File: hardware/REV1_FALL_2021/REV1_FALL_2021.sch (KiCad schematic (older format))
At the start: 28 parts, among them J101 Screw_Terminal_01x02, J102 Screw_Terminal_01x02, Q101 Q_NMOS_GDS, Q102 Q_NMOS_GDS, U1 Teensy3.6_All_Pins, U2 PA16165_Breakout, U3 MPL3115A2_Breakout, U4 BNO055_Breakout, U5 RFM69HCW_Breakout

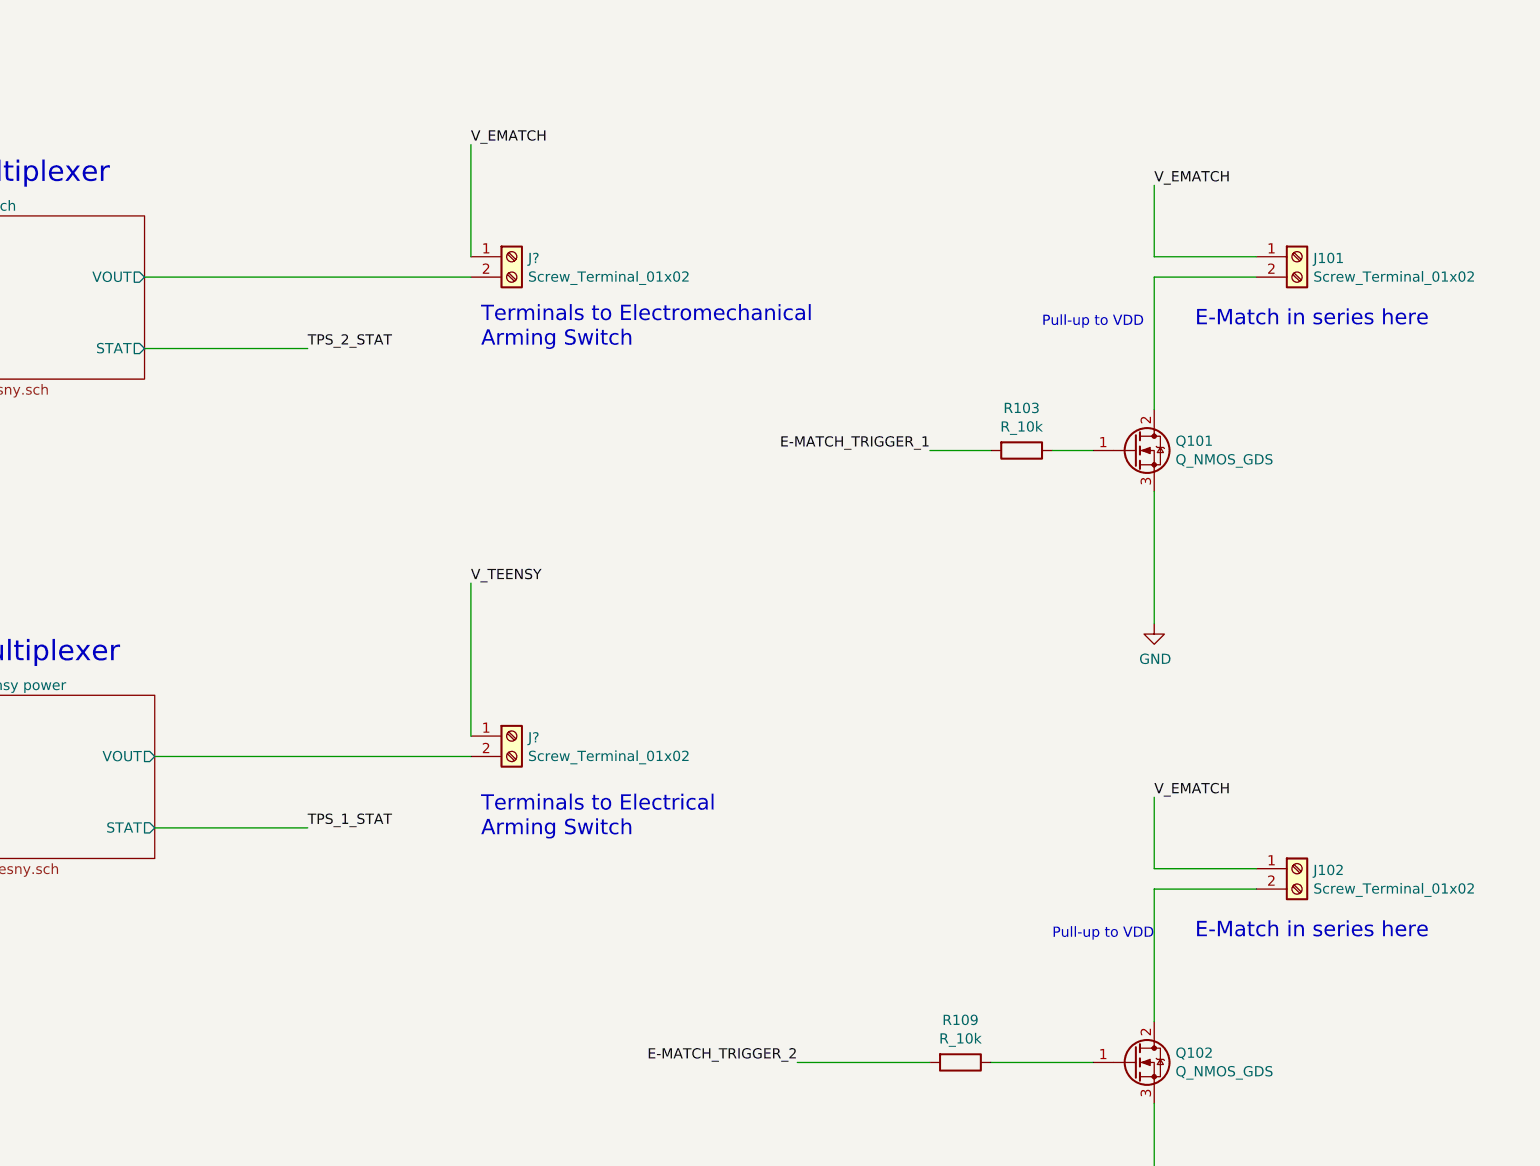
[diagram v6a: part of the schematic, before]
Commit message: add additional solderable terminals to arming switches and ematch connections
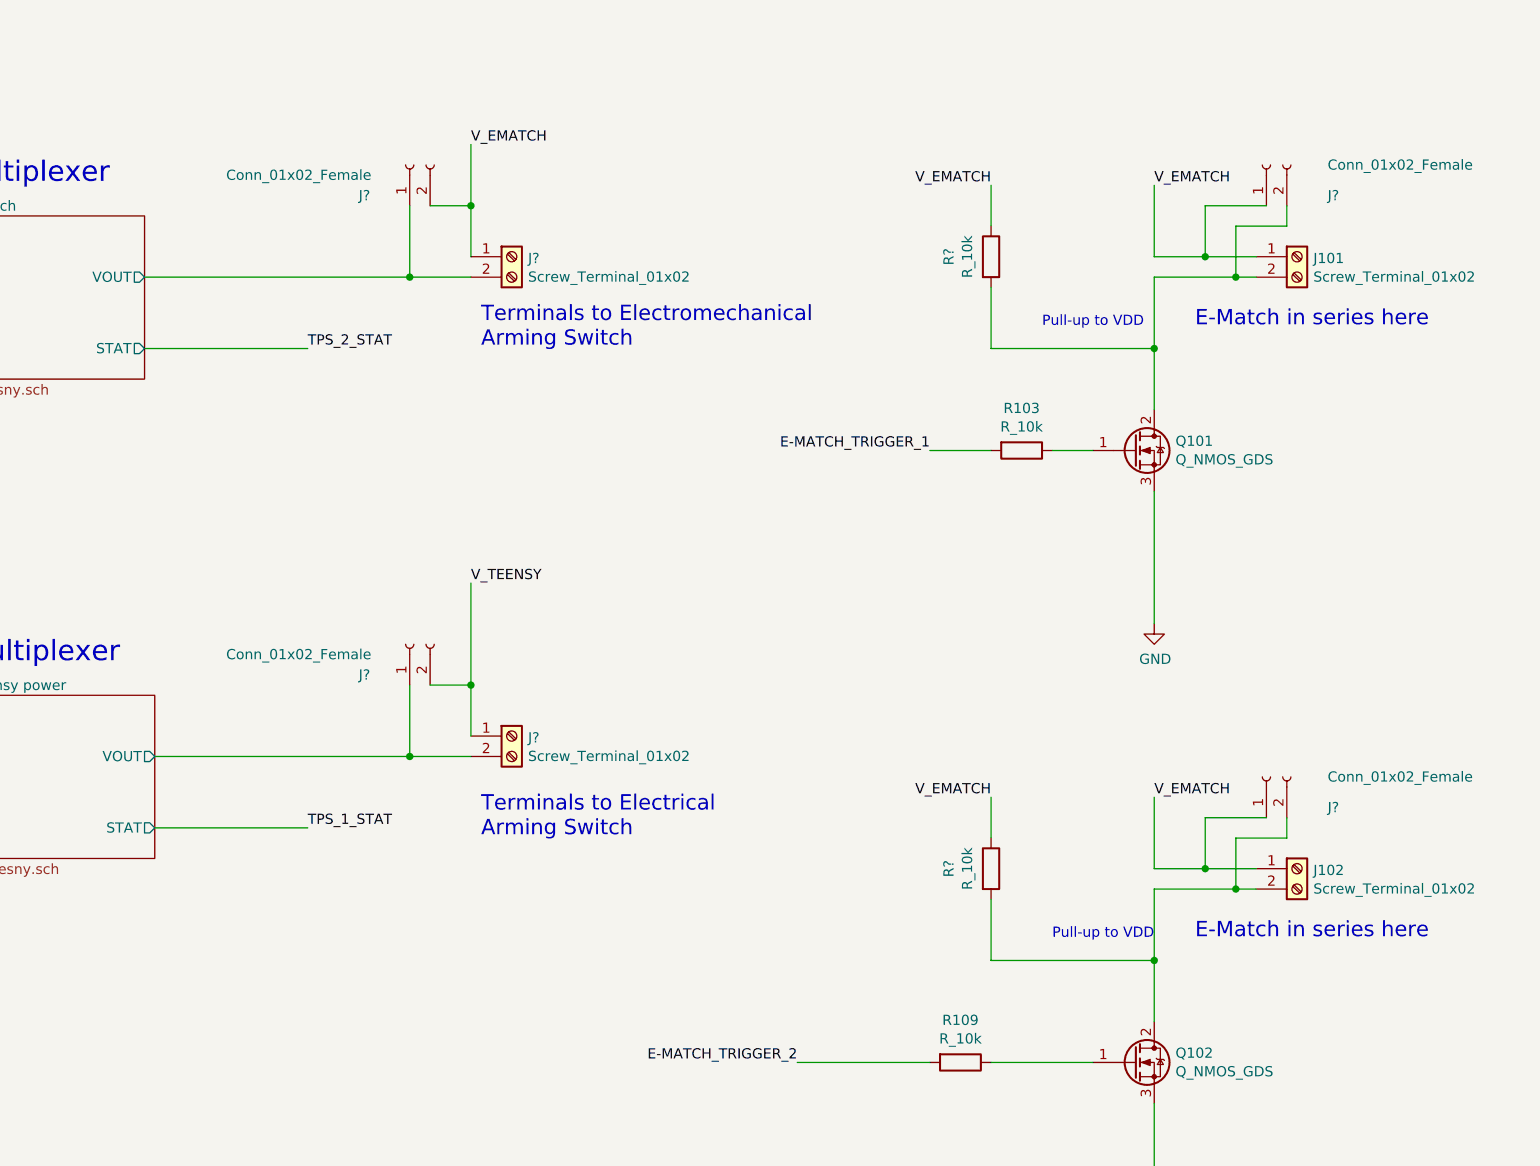
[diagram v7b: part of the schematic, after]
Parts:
- added J? (x4): Conn_01x02_Female, Connector_Wire:SolderWire-1sqmm_1x02_P5.4mm_D1.4mm_OD2.7mm_Relief2x, symbol Connector:Conn_01x02_Female
- added R? (x2): R_10k, Resistor_SMD:R_0805_2012Metric_Pad1.20x1.40mm_HandSolder, symbol Device:R
- J? (x2): footprint (none) -> TerminalBlock:TerminalBlock_bornier-2_P5.08mm
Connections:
- net TPS2113A for E-match/VOUT: now also J?.1 (Pin_1)
- net TPS2113A for Teensy power/VOUT: now also J?.1 (Pin_1)
- net V_EMATCH: now also J?.1 (Pin_1), J?.1 (Pin_1), J?.2 (Pin_2), R?.1, R?.1
- net V_TEENSY: now also J?.2 (Pin_2)
- net at J101.2 (Pin_2), Q101.2 (D): now also J?.2 (Pin_2), R?.2
- net at J102.2 (Pin_2), Q102.2 (D): now also J?.2 (Pin_2), R?.2
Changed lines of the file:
@@
 	21050 2600 21050 2250
 Wire Wire Line
-	21550 2600 21050 2600
-Wire Wire Line
-	21050 2700 21550 2700
+	21550 2600 21300 2600
+Wire Wire Line
+	21050 2700 21450 2700
 $Comp
 L power:GND #PWR0112
@@
 $EndComp
 Wire Wire Line
-	21050 3350 21050 2700
+	21050 3350 21050 3050
 Wire Wire Line
 	21050 4400 21050 3750
@@
 	21050 5600 21050 5250
 Wire Wire Line
-	21550 5600 21050 5600
-Wire Wire Line
-	21050 5700 21550 5700
+	21550 5600 21300 5600
+Wire Wire Line
+	21050 5700 21450 5700
 $Comp
 L power:GND #PWR0108
@@
 	1    0    0    -1
 $EndComp
-Wire Wire Line
-	21050 6350 21050 5700
 Wire Wire Line
 	21050 7400 21050 6750
@@
 F 0 "J?" H 17980 2592 50  0000 L CNN
 F 1 "Screw_Terminal_01x02" H 17980 2501 50  0000 L CNN
-F 2 "" H 17900 2600 50  0001 C CNN
+F 2 "TerminalBlock:TerminalBlock_bornier-2_P5.08mm" H 17900 2600 50  0001 C CNN
 F 3 "~" H 17900 2600 50  0001 C CNN
 	1    17900 2600
@@
 $EndComp
 Wire Wire Line
-	16100 2700 17700 2700
-Wire Wire Line
-	17700 2600 17700 2050
+	16100 2700 17400 2700
+Wire Wire Line
+	17700 2600 17700 2350
 Text Notes 17750 3050 0    75   ~ 0
 Terminals to Electromechanical \nArming Switch
@@
 F 0 "J?" H 17980 4942 50  0000 L CNN
 F 1 "Screw_Terminal_01x02" H 17980 4851 50  0000 L CNN
-F 2 "" H 17900 4950 50  0001 C CNN
+F 2 "TerminalBlock:TerminalBlock_bornier-2_P5.08mm" H 17900 4950 50  0001 C CNN
 F 3 "~" H 17900 4950 50  0001 C CNN
 	1    17900 4950
@@
 $EndComp
 Wire Wire Line
-	16150 5050 17700 5050
-Wire Wire Line
-	17700 4950 17700 4200
+	16150 5050 17400 5050
+Wire Wire Line
+	17700 4950 17700 4700
 Text Notes 17750 5450 0    75   ~ 0
 Terminals to Electrical \nArming Switch
@@
 	14350 3050 14700 3050
 NoConn ~ 1350 4750
+$Comp
+L Connector:Conn_01x02_Female J?
+U 1 1 61EE6B30
+P 17400 2150
+F 0 "J?" V 17250 2400 50  0000 R CNN
+F 1 "Conn_01x02_Female" V 17350 3050 50  0000 R CNN
+F 2 "Connector_Wire:SolderWire-1sqmm_1x02_P5.4mm_D1.4mm_OD2.7mm_Relief2x" H 17400 2150 50  0001 C CNN
+F 3 "~" H 17400 2150 50  0001 C CNN
+	1    17400 2150
+	0    -1   -1   0
+$EndComp
+Wire Wire Line
+	17500 2350 17700 2350
+Connection ~ 17700 2350
+Wire Wire Line
+	17700 2350 17700 2050
+Wire Wire Line
+	17400 2350 17400 2700
+Connection ~ 17400 2700
+Wire Wire Line
+	17400 2700 17700 2700
+$Comp
+L Connector:Conn_01x02_Female J?
+U 1 1 61EF490E
+P 17400 4500
+F 0 "J?" V 17250 4750 50  0000 R CNN
+F 1 "Conn_01x02_Female" V 17350 5400 50  0000 R CNN
+F 2 "Connector_Wire:SolderWire-1sqmm_1x02_P5.4mm_D1.4mm_OD2.7mm_Relief2x" H 17400 4500 50  0001 C CNN
+F 3 "~" H 17400 4500 50  0001 C CNN
+	1    17400 4500
+	0    -1   -1   0
+$EndComp
+Wire Wire Line
+	17500 4700 17700 4700
+Connection ~ 17700 4700
+Wire Wire Line
+	17700 4700 17700 4200
+Wire Wire Line
+	17400 4700 17400 5050
+Connection ~ 17400 5050
+Wire Wire Line
+	17400 5050 17700 5050
+$Comp
+L Device:R R?
+U 1 1 61EFFA45
+P 20250 2600
+F 0 "R?" V 20043 2600 50  0000 C CNN
+F 1 "R_10k" V 20134 2600 50  0000 C CNN
+F 2 "Resistor_SMD:R_0805_2012Metric_Pad1.20x1.40mm_HandSolder" V 20180 2600 50  0001 C CNN
+F 3 "~" H 20250 2600 50  0001 C CNN
+	1    20250 2600
+	1    0    0    -1
+$EndComp
+Wire Wire Line
+	20250 2750 20250 3050
+Wire Wire Line
+	20250 3050 21050 3050
+Connection ~ 21050 3050
+Wire Wire Line
+	21050 3050 21050 2700
+Text Label 20250 2250 2    50   ~ 0
+V_EMATCH
+Wire Wire Line
+	20250 2450 20250 2250
+$Comp
+L Device:R R?
+U 1 1 61F0973E
+P 20250 5600
+F 0 "R?" V 20043 5600 50  0000 C CNN
+F 1 "R_10k" V 20134 5600 50  0000 C CNN
+F 2 "Resistor_SMD:R_0805_2012Metric_Pad1.20x1.40mm_HandSolder" V 20180 5600 50  0001 C CNN
+F 3 "~" H 20250 5600 50  0001 C CNN
+	1    20250 5600
+	1    0    0    -1
+$EndComp
+Text Label 20250 5250 2    50   ~ 0
+V_EMATCH
+Wire Wire Line
+	20250 5250 20250 5450
+Wire Wire Line
+	21050 5700 21050 6050
+Wire Wire Line
+	21050 6050 20250 6050
+Wire Wire Line
+	20250 6050 20250 5750
+Connection ~ 21050 6050
+Wire Wire Line
+	21050 6050 21050 6350
+$Comp
+L Connector:Conn_01x02_Female J?
+U 1 1 61F16DD4
+P 21600 2150
+F 0 "J?" V 21450 1850 50  0000 R CNN
+F 1 "Conn_01x02_Female" V 21600 1850 50  0000 R CNN
+F 2 "Connector_Wire:SolderWire-1sqmm_1x02_P5.4mm_D1.4mm_OD2.7mm_Relief2x" H 21600 2150 50  0001 C CNN
+F 3 "~" H 21600 2150 50  0001 C CNN
+	1    21600 2150
+	0    -1   -1   0
+$EndComp
+Wire Wire Line
+	21600 2350 21300 2350
+Wire Wire Line
+	21300 2350 21300 2600
+Connection ~ 21300 2600
+Wire Wire Line
+	21300 2600 21050 2600
+Wire Wire Line
+	21700 2350 21700 2450
+Wire Wire Line
+	21700 2450 21450 2450
+Wire Wire Line
+	21450 2450 21450 2700
+Connection ~ 21450 2700
+Wire Wire Line
+	21450 2700 21550 2700
+$Comp
+L Connector:Conn_01x02_Female J?
+U 1 1 61F21E7F
+P 21600 5150
+F 0 "J?" V 21450 4850 50  0000 R CNN
+F 1 "Conn_01x02_Female" V 21600 4850 50  0000 R CNN
+F 2 "Connector_Wire:SolderWire-1sqmm_1x02_P5.4mm_D1.4mm_OD2.7mm_Relief2x" H 21600 5150 50  0001 C CNN
+F 3 "~" H 21600 5150 50  0001 C CNN
+	1    21600 5150
+	0    -1   -1   0
+$EndComp
+Wire Wire Line
+	21300 5600 21300 5350
+Wire Wire Line
+	21300 5350 21600 5350
+Connection ~ 21300 5600
+Wire Wire Line
+	21300 5600 21050 5600
+Wire Wire Line
+	21700 5350 21700 5450
+Wire Wire Line
+	21700 5450 21450 5450
+Wire Wire Line
+	21450 5450 21450 5700
+Connection ~ 21450 5700
+Wire Wire Line
+	21450 5700 21550 5700
 $EndSCHEMATC

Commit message: add digital key switch connection to Teensy with pull-down resistor
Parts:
- added J103: Conn_01x02_Female, Connector_Wire:SolderWire-1sqmm_1x02_P5.4mm_D1.4mm_OD2.7mm_Relief2x, symbol Connector:Conn_01x02_Female
- added J104: Screw_Terminal_01x02, TerminalBlock:TerminalBlock_bornier-2_P5.08mm, symbol Connector:Screw_Terminal_01x02
- added R110: R_10k, Resistor_SMD:R_0805_2012Metric_Pad1.20x1.40mm_HandSolder, symbol Device:R
- gave numbers to parts that had none: 8
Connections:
- net 3.3V: now also J103.1 (Pin_1), J104.1 (Pin_1)
- net GND: now also R110.2
- net KEY_SWITCH_DIGITAL: now reaches U1.34 (37_A18_PWM_SCL1)
- net KEY_SWITCH_DIGITAL: now also J103.2 (Pin_2), J104.2 (Pin_2), R110.1
- no-connect marks 85 -> 84
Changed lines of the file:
@@
 Text Notes 21250 2950 0    75   ~ 0
 E-Match in series here
-Text Label 21050 2250 0    50   ~ 0
-V_EMATCH
-Wire Wire Line
-	21050 2600 21050 2250
-Wire Wire Line
-	21550 2600 21300 2600
-Wire Wire Line
-	21050 2700 21450 2700
 $Comp
 L power:GND #PWR0112
@@
 Wire Wire Line
 	21050 4400 21050 3750
-$Comp
-L Connector:Screw_Terminal_01x02 J101
-U 1 1 61A64E05
-P 21750 2600
-F 0 "J101" H 21830 2592 50  0000 L CNN
-F 1 "Screw_Terminal_01x02" H 21830 2501 50  0000 L CNN
-F 2 "TerminalBlock:TerminalBlock_bornier-2_P5.08mm" H 21750 2600 50  0001 C CNN
-F 3 "~" H 21750 2600 50  0001 C CNN
-	1    21750 2600
-	1    0    0    -1
-$EndComp
 Wire Wire Line
 	20550 3550 20750 3550
@@
 $EndComp
 $Comp
-L Connector:Screw_Terminal_01x02 J?
+L Connector:Screw_Terminal_01x02 J107
 U 1 1 61BAEBD9
 P 17900 2600
-F 0 "J?" H 17980 2592 50  0000 L CNN
+F 0 "J107" H 17980 2592 50  0000 L CNN
 F 1 "Screw_Terminal_01x02" H 17980 2501 50  0000 L CNN
 F 2 "TerminalBlock:TerminalBlock_bornier-2_P5.08mm" H 17900 2600 50  0001 C CNN
@@
 Terminals to Electromechanical \nArming Switch
 $Comp
-L Connector:Screw_Terminal_01x02 J?
+L Connector:Screw_Terminal_01x02 J108
 U 1 1 61BB7A24
 P 17900 4950
-F 0 "J?" H 17980 4942 50  0000 L CNN
+F 0 "J108" H 17980 4942 50  0000 L CNN
 F 1 "Screw_Terminal_01x02" H 17980 4851 50  0000 L CNN
 F 2 "TerminalBlock:TerminalBlock_bornier-2_P5.08mm" H 17900 4950 50  0001 C CNN
@@
 Wire Wire Line
 	14350 3050 14700 3050
-NoConn ~ 1350 4750
-$Comp
-L Connector:Conn_01x02_Female J?
+$Comp
+L Connector:Conn_01x02_Female J105
 U 1 1 61EE6B30
 P 17400 2150
-F 0 "J?" V 17250 2400 50  0000 R CNN
+F 0 "J105" V 17250 2400 50  0000 R CNN
 F 1 "Conn_01x02_Female" V 17350 3050 50  0000 R CNN
 F 2 "Connector_Wire:SolderWire-1sqmm_1x02_P5.4mm_D1.4mm_OD2.7mm_Relief2x" H 17400 2150 50  0001 C CNN
@@
 	17400 2700 17700 2700
 $Comp
-L Connector:Conn_01x02_Female J?
+L Connector:Conn_01x02_Female J106
 U 1 1 61EF490E
 P 17400 4500
-F 0 "J?" V 17250 4750 50  0000 R CNN
+F 0 "J106" V 17250 4750 50  0000 R CNN
 F 1 "Conn_01x02_Female" V 17350 5400 50  0000 R CNN
 F 2 "Connector_Wire:SolderWire-1sqmm_1x02_P5.4mm_D1.4mm_OD2.7mm_Relief2x" H 17400 4500 50  0001 C CNN
@@
 	17400 5050 17700 5050
 $Comp
-L Device:R R?
+L Device:R R111
 U 1 1 61EFFA45
 P 20250 2600
-F 0 "R?" V 20043 2600 50  0000 C CNN
+F 0 "R111" V 20043 2600 50  0000 C CNN
 F 1 "R_10k" V 20134 2600 50  0000 C CNN
 F 2 "Resistor_SMD:R_0805_2012Metric_Pad1.20x1.40mm_HandSolder" V 20180 2600 50  0001 C CNN
@@
 Wire Wire Line
 	20250 3050 21050 3050
-Connection ~ 21050 3050
-Wire Wire Line
-	21050 3050 21050 2700
 Text Label 20250 2250 2    50   ~ 0
 V_EMATCH
@@
 	20250 2450 20250 2250
 $Comp
-L Device:R R?
+L Device:R R112
 U 1 1 61F0973E
 P 20250 5600
-F 0 "R?" V 20043 5600 50  0000 C CNN
+F 0 "R112" V 20043 5600 50  0000 C CNN
 F 1 "R_10k" V 20134 5600 50  0000 C CNN
 F 2 "Resistor_SMD:R_0805_2012Metric_Pad1.20x1.40mm_HandSolder" V 20180 5600 50  0001 C CNN
@@
 	21050 6050 21050 6350
 $Comp
-L Connector:Conn_01x02_Female J?
+L Connector:Conn_01x02_Female J110
+U 1 1 61F21E7F
+P 21600 5150
+F 0 "J110" V 21450 4850 50  0000 R CNN
+F 1 "Conn_01x02_Female" V 21600 4850 50  0000 R CNN
+F 2 "Connector_Wire:SolderWire-1sqmm_1x02_P5.4mm_D1.4mm_OD2.7mm_Relief2x" H 21600 5150 50  0001 C CNN
+F 3 "~" H 21600 5150 50  0001 C CNN
+	1    21600 5150
+	0    -1   -1   0
+$EndComp
+Wire Wire Line
+	21300 5600 21300 5350
+Wire Wire Line
+	21300 5350 21600 5350
+Connection ~ 21300 5600
+Wire Wire Line
+	21300 5600 21050 5600
+Wire Wire Line
+	21700 5350 21700 5450
+Wire Wire Line
+	21700 5450 21450 5450
+Wire Wire Line
+	21450 5450 21450 5700
+Connection ~ 21450 5700
+Wire Wire Line
+	21450 5700 21550 5700
+Wire Wire Line
+	21450 2700 21550 2700
+Wire Wire Line
+	21450 2450 21450 2700
+Wire Wire Line
+	21700 2450 21450 2450
+Wire Wire Line
+	21700 2350 21700 2450
+Wire Wire Line
+	21300 2600 21050 2600
+Wire Wire Line
+	21300 2350 21300 2600
+Wire Wire Line
+	21600 2350 21300 2350
+$Comp
+L Connector:Conn_01x02_Female J109
 U 1 1 61F16DD4
 P 21600 2150
-F 0 "J?" V 21450 1850 50  0000 R CNN
+F 0 "J109" V 21450 1850 50  0000 R CNN
 F 1 "Conn_01x02_Female" V 21600 1850 50  0000 R CNN
 F 2 "Connector_Wire:SolderWire-1sqmm_1x02_P5.4mm_D1.4mm_OD2.7mm_Relief2x" H 21600 2150 50  0001 C CNN
@@
 	0    -1   -1   0
 $EndComp
-Wire Wire Line
-	21600 2350 21300 2350
-Wire Wire Line
-	21300 2350 21300 2600
+Connection ~ 21050 3050
+Wire Wire Line
+	21050 3050 21050 2700
+$Comp
+L Connector:Screw_Terminal_01x02 J101
+U 1 1 61A64E05
+P 21750 2600
+F 0 "J101" H 21830 2592 50  0000 L CNN
+F 1 "Screw_Terminal_01x02" H 21830 2501 50  0000 L CNN
+F 2 "TerminalBlock:TerminalBlock_bornier-2_P5.08mm" H 21750 2600 50  0001 C CNN
+F 3 "~" H 21750 2600 50  0001 C CNN
+	1    21750 2600
+	1    0    0    -1
+$EndComp
+Connection ~ 21450 2700
+Wire Wire Line
+	21050 2700 21450 2700
 Connection ~ 21300 2600
 Wire Wire Line
-	21300 2600 21050 2600
-Wire Wire Line
-	21700 2350 21700 2450
-Wire Wire Line
-	21700 2450 21450 2450
-Wire Wire Line
-	21450 2450 21450 2700
-Connection ~ 21450 2700
-Wire Wire Line
-	21450 2700 21550 2700
-$Comp
-L Connector:Conn_01x02_Female J?
-U 1 1 61F21E7F
-P 21600 5150
-F 0 "J?" V 21450 4850 50  0000 R CNN
-F 1 "Conn_01x02_Female" V 21600 4850 50  0000 R CNN
-F 2 "Connector_Wire:SolderWire-1sqmm_1x02_P5.4mm_D1.4mm_OD2.7mm_Relief2x" H 21600 5150 50  0001 C CNN
-F 3 "~" H 21600 5150 50  0001 C CNN
-	1    21600 5150
-	0    -1   -1   0
-$EndComp
-Wire Wire Line
-	21300 5600 21300 5350
-Wire Wire Line
-	21300 5350 21600 5350
-Connection ~ 21300 5600
-Wire Wire Line
-	21300 5600 21050 5600
-Wire Wire Line
-	21700 5350 21700 5450
-Wire Wire Line
-	21700 5450 21450 5450
-Wire Wire Line
-	21450 5450 21450 5700
-Connection ~ 21450 5700
-Wire Wire Line
-	21450 5700 21550 5700
+	21550 2600 21300 2600
+Wire Wire Line
+	21050 2600 21050 2250
+Text Label 21050 2250 0    50   ~ 0
+V_EMATCH
+$Comp
+L Connector:Screw_Terminal_01x02 J104
+U 1 1 61F48A1B
+P 6600 9300
+F 0 "J104" H 6680 9292 50  0000 L CNN
+F 1 "Screw_Terminal_01x02" H 6680 9201 50  0000 L CNN
+F 2 "TerminalBlock:TerminalBlock_bornier-2_P5.08mm" H 6600 9300 50  0001 C CNN
+F 3 "~" H 6600 9300 50  0001 C CNN
+	1    6600 9300
+	1    0    0    -1
+$EndComp
+$Comp
+L Device:R R110
+U 1 1 61F4F9C8
+P 5700 9700
+F 0 "R110" V 5493 9700 50  0000 C CNN
+F 1 "R_10k" V 5584 9700 50  0000 C CNN
+F 2 "Resistor_SMD:R_0805_2012Metric_Pad1.20x1.40mm_HandSolder" V 5630 9700 50  0001 C CNN
+F 3 "~" H 5700 9700 50  0001 C CNN
+	1    5700 9700
+	1    0    0    -1
+$EndComp
+$Comp
+L power:GND #PWR0114
+U 1 1 61F569C1
+P 5700 10050
+F 0 "#PWR0114" H 5700 9800 50  0001 C CNN
+F 1 "GND" H 5705 9877 50  0000 C CNN
+F 2 "" H 5700 10050 50  0001 C CNN
+F 3 "" H 5700 10050 50  0001 C CNN
+	1    5700 10050
+	1    0    0    -1
+$EndComp
+Text Label 5450 9400 2    50   ~ 0
+KEY_SWITCH_DIGITAL
+Wire Wire Line
+	5450 9400 5700 9400
+Wire Wire Line
+	5700 9400 5700 9550
+Connection ~ 5700 9400
+Wire Wire Line
+	5700 9850 5700 10050
+Wire Wire Line
+	5700 9400 6100 9400
+$Comp
+L Connector:Conn_01x02_Female J103
+U 1 1 61F48A22
+P 6000 8400
+F 0 "J103" V 5850 8100 50  0000 R CNN
+F 1 "Conn_01x02_Female" V 6000 8100 50  0000 R CNN
+F 2 "Connector_Wire:SolderWire-1sqmm_1x02_P5.4mm_D1.4mm_OD2.7mm_Relief2x" H 6000 8400 50  0001 C CNN
+F 3 "~" H 6000 8400 50  0001 C CNN
+	1    6000 8400
+	0    -1   -1   0
+$EndComp
+Wire Wire Line
+	6400 9300 6250 9300
+Wire Wire Line
+	6250 9300 6250 8850
+Wire Wire Line
+	6250 8850 6000 8850
+Wire Wire Line
+	6000 8600 6000 8850
+Connection ~ 6000 8850
+Wire Wire Line
+	6000 8850 5450 8850
+Wire Wire Line
+	6100 8600 6100 9400
+Connection ~ 6100 9400
+Wire Wire Line
+	6100 9400 6400 9400
+Text Label 5450 8850 2    50   ~ 0
+3.3V
+Text Label 1350 4750 2    50   ~ 0
+KEY_SWITCH_DIGITAL
 $EndSCHEMATC
